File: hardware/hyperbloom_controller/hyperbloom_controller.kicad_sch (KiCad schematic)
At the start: 11 parts, among them J1 SMA glitch connector, J2 glitch pin, J3 Left side header, J4 Right side header, Q1 IRLML2502TRPbF, Q2 IRF8714PbF

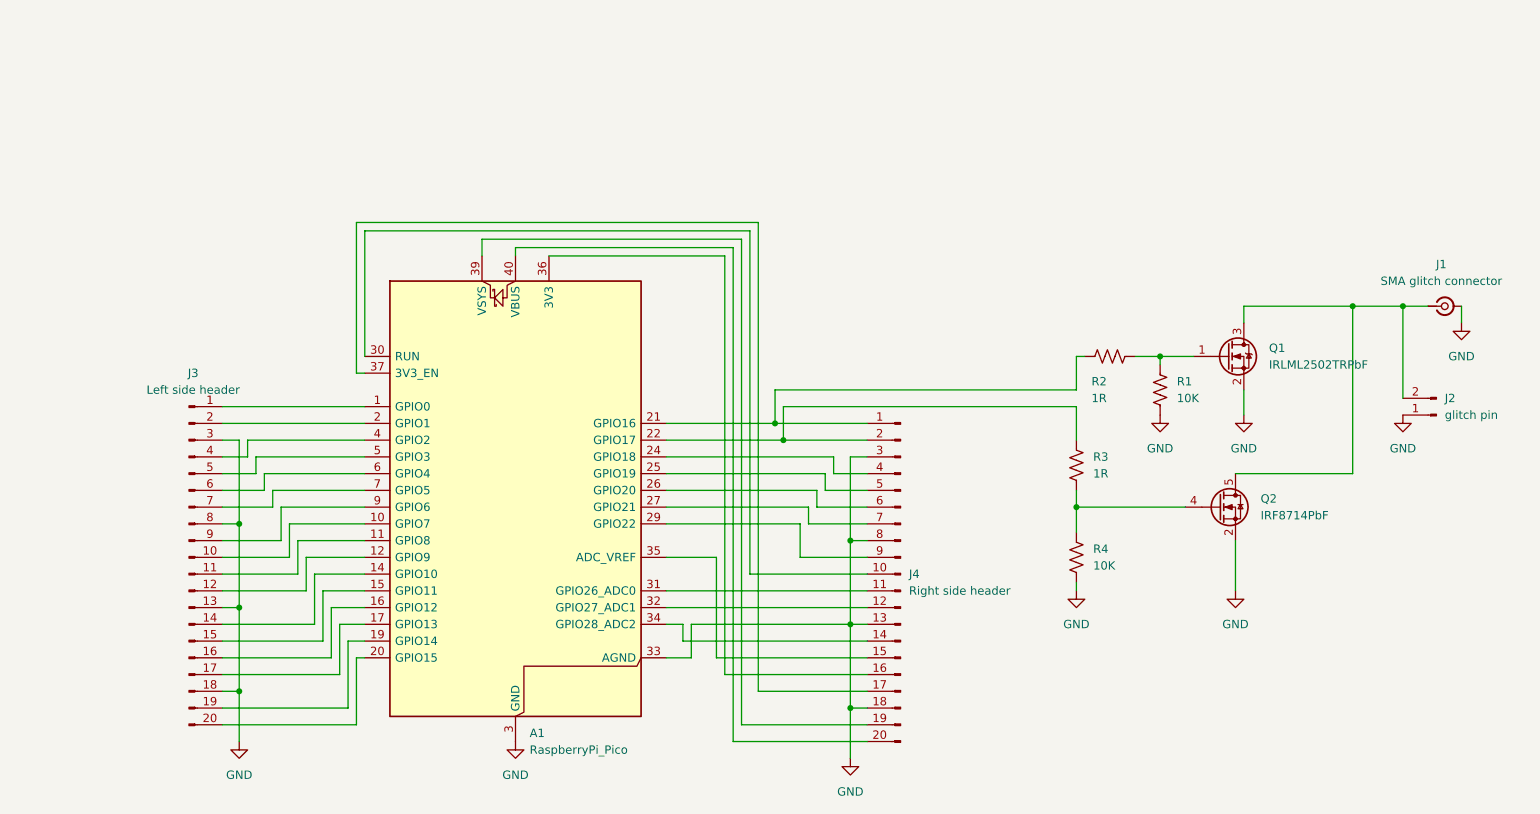
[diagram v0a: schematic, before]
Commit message: Controller PCB v0.1
I designed this a while ago but forgot to commit

Mainly just cleaned up the routing
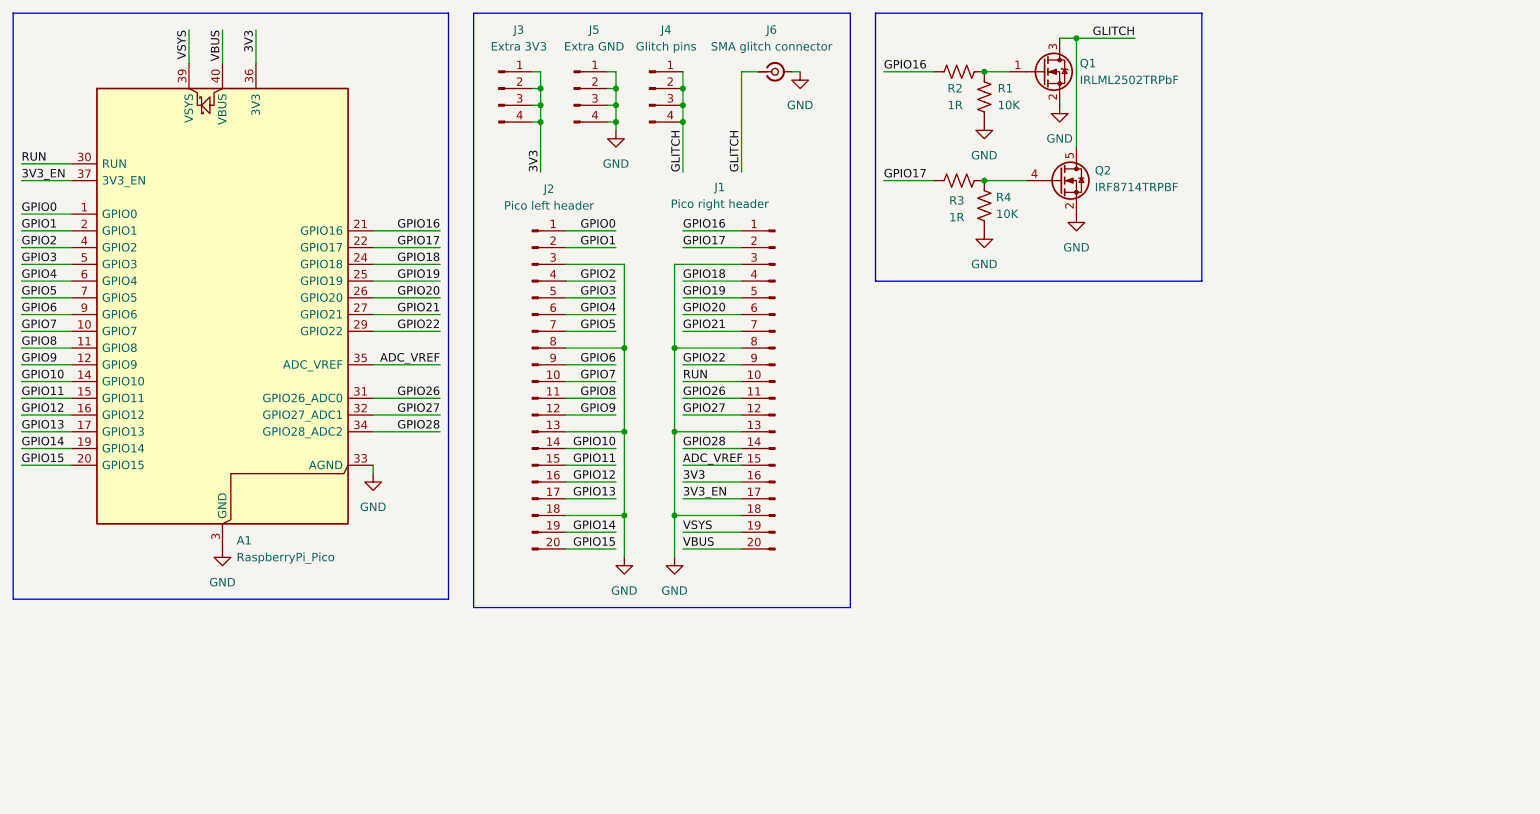
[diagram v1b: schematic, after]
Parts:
- removed J1: SMA glitch connector, Connector_Coaxial:SMA_Amphenol_132289_EdgeMount, symbol Connector:Conn_Coaxial_Small
- removed J2: glitch pin, Connector_PinHeader_2.54mm:PinHeader_1x02_P2.54mm_Vertical, symbol Connector:Conn_01x02_Pin
- added J3: Extra 3V3, Connector_PinHeader_2.54mm:PinHeader_1x04_P2.54mm_Vertical, symbol Connector:Conn_01x04_Pin
- added J4: Glitch pins, Connector_PinHeader_2.54mm:PinHeader_1x04_P2.54mm_Vertical, symbol Connector:Conn_01x04_Pin
- added J5: Extra GND, Connector_PinHeader_2.54mm:PinHeader_1x04_P2.54mm_Vertical, symbol Connector:Conn_01x04_Pin
- added J6: SMA glitch connector, Connector_Coaxial:SMA_Amphenol_901-144_Vertical, symbol Connector:Conn_Coaxial_Small
- J1: renamed from J4; value Right side header -> Pico right header
- J2: renamed from J3; value Left side header -> Pico left header
- Q2: value IRF8714PbF -> IRF8714TRPBF
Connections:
- net GND: now also J5.1 (Pin_1), J5.2 (Pin_2), J5.3 (Pin_3), J5.4 (Pin_4), J6.2 (Ext)
- net GPIO0: now reaches A1.1 (GPIO0), J2.1 (Pin_1)
- net GPIO7: now reaches A1.10 (GPIO7), J2.10 (Pin_10)
- net GPIO8: now reaches A1.11 (GPIO8), J2.11 (Pin_11)
- net GPIO9: now reaches A1.12 (GPIO9), J2.12 (Pin_12)
- net GPIO10: now reaches A1.14 (GPIO10), J2.14 (Pin_14)
- net GPIO11: now reaches A1.15 (GPIO11), J2.15 (Pin_15)
- net GPIO12: now reaches A1.16 (GPIO12), J2.16 (Pin_16)
- net GPIO13: now reaches A1.17 (GPIO13), J2.17 (Pin_17)
- net GPIO14: now reaches A1.19 (GPIO14), J2.19 (Pin_19)
- net GPIO1: now reaches A1.2 (GPIO1), J2.2 (Pin_2)
- net GPIO15: now reaches A1.20 (GPIO15), J2.20 (Pin_20)
- net GPIO2: now reaches A1.4 (GPIO2), J2.4 (Pin_4)
- net GPIO3: now reaches A1.5 (GPIO3), J2.5 (Pin_5)
- net GPIO4: now reaches A1.6 (GPIO4), J2.6 (Pin_6)
- net GPIO5: now reaches A1.7 (GPIO5), J2.7 (Pin_7)
- net GPIO6: now reaches A1.9 (GPIO6), J2.9 (Pin_9)
- net GLITCH: now reaches Q1.3 (D), Q2.5 (D), Q2.6 (D), Q2.7 (D), Q2.8 (D)
- net GLITCH: now also J4.1 (Pin_1), J4.2 (Pin_2), J4.3 (Pin_3), J4.4 (Pin_4), J6.1 (In)
- net GPIO17: now reaches A1.22 (GPIO17), J1.2 (Pin_2), R3.1
- net GPIO16: now reaches A1.21 (GPIO16), J1.1 (Pin_1), R2.1
- net GPIO18: now reaches A1.24 (GPIO18), J1.4 (Pin_4)
- net GPIO19: now reaches A1.25 (GPIO19), J1.5 (Pin_5)
- net GPIO20: now reaches A1.26 (GPIO20), J1.6 (Pin_6)
- net GPIO21: now reaches A1.27 (GPIO21), J1.7 (Pin_7)
- net GPIO22: now reaches A1.29 (GPIO22), J1.9 (Pin_9)
- net RUN: now reaches A1.30 (RUN), J1.10 (Pin_10)
- net GPIO26: now reaches A1.31 (GPIO26_ADC0), J1.11 (Pin_11)
- net GPIO27: now reaches A1.32 (GPIO27_ADC1), J1.12 (Pin_12)
- net GPIO28: now reaches A1.34 (GPIO28_ADC2), J1.14 (Pin_14)
- net ADC_VREF: now reaches A1.35 (ADC_VREF), J1.15 (Pin_15)
- net 3V3: now reaches A1.36 (3V3), J1.16 (Pin_16)
- net 3V3: now also J3.1 (Pin_1), J3.2 (Pin_2), J3.3 (Pin_3), J3.4 (Pin_4)
- net 3V3_EN: now reaches A1.37 (3V3_EN), J1.17 (Pin_17)
- net VSYS: now reaches A1.39 (VSYS), J1.19 (Pin_19)
- net VBUS: now reaches A1.40 (VBUS), J1.20 (Pin_20)
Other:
- moved on the sheet: A1, J1, J2, Q1, Q2, R1, R2, R3, R4
